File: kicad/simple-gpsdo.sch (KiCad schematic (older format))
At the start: 93 parts, among them J1 PPS_OUT, J2 PWR, J3 ISP, J6 USB_B_Micro, J7 NEO-6M, J8 10MHz_OUT, Q1 PJA3407, SW1 RST, U1 XRP6272ITC5TR-F, U2 ATmega32U4-AU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

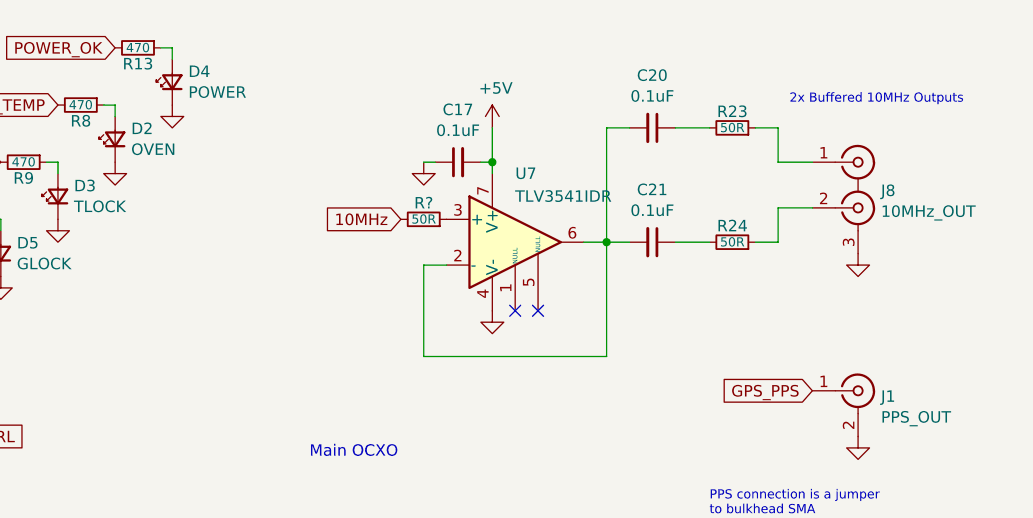
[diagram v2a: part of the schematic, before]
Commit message: final schematic updates for new buffer amplifier
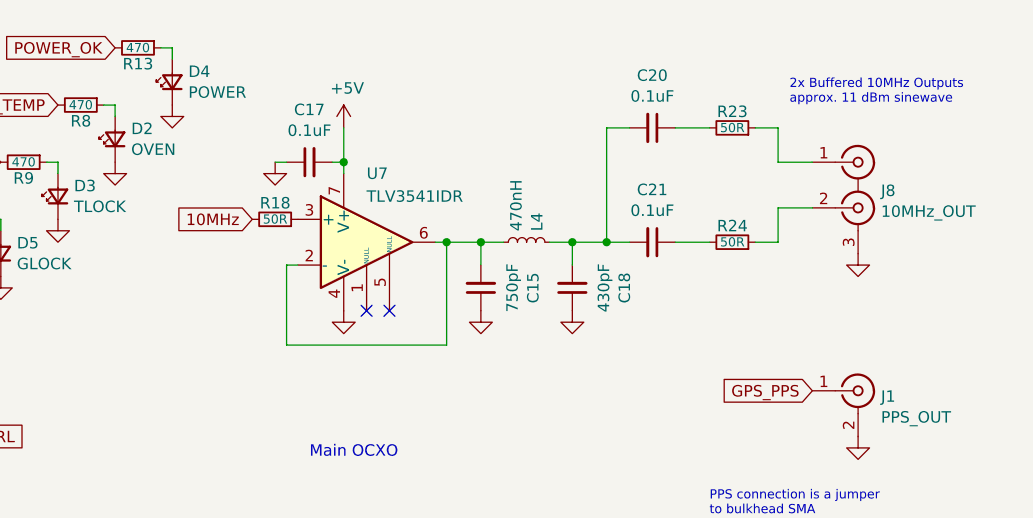
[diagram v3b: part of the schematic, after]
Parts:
- added C15: 750pF, Capacitor_SMD:C_0805_2012Metric_Pad1.15x1.40mm_HandSolder, symbol Device:C_Small
- added C18: 430pF, Capacitor_SMD:C_0805_2012Metric_Pad1.15x1.40mm_HandSolder, symbol Device:C_Small
- added L4: 470nH, Inductor_SMD:L_1206_3216Metric_Pad1.42x1.75mm_HandSolder, symbol Device:L_Small
- gave numbers to parts that had none: 1
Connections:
- net GND: now also C15.1, C18.1
- net at U7.2 (-), U7.6: now also C15.2, L4.2; no longer C20.2, C21.2
- new net: C18.2, C20.2, C21.2, L4.1
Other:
- note added: "2x Buffered 10MHz Outputs\napprox. 11 dBm sinewave"
- note removed: "2x Buffered 10MHz Outputs"
- moved on the sheet: C17, R18, U7
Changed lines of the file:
@@
 L Amplifier_Operational:AD8610 U7
 U 1 1 5F779082
-P 8000 1850
-F 0 "U7" H 8000 2150 50  0000 L CNN
-F 1 "TLV3541IDR" H 8000 2050 50  0000 L CNN
-F 2 "Package_SO:SOIC-8_3.9x4.9mm_P1.27mm" H 8050 1900 50  0001 C CNN
-F 3 "https://www.analog.com/media/en/technical-documentation/data-sheets/AD8610_8620.pdf" H 8150 2000 50  0001 C CNN
-	1    8000 1850
+P 7350 1850
+F 0 "U7" H 7350 2150 50  0000 L CNN
+F 1 "TLV3541IDR" H 7350 2050 50  0000 L CNN
+F 2 "Package_SO:SOIC-8_3.9x4.9mm_P1.27mm" H 7400 1900 50  0001 C CNN
+F 3 "https://www.analog.com/media/en/technical-documentation/data-sheets/AD8610_8620.pdf" H 7500 2000 50  0001 C CNN
+	1    7350 1850
 	1    0    0    -1
 $EndComp
@@
 L power:GND #PWR043
 U 1 1 5F857189
-P 7600 1500
-F 0 "#PWR043" H 7600 1250 50  0001 C CNN
-F 1 "GND" H 7605 1327 50  0001 C CNN
-F 2 "" H 7600 1500 50  0001 C CNN
-F 3 "" H 7600 1500 50  0001 C CNN
-	1    7600 1500
+P 6950 1500
+F 0 "#PWR043" H 6950 1250 50  0001 C CNN
+F 1 "GND" H 6955 1327 50  0001 C CNN
+F 2 "" H 6950 1500 50  0001 C CNN
+F 3 "" H 6950 1500 50  0001 C CNN
+	1    6950 1500
 	1    0    0    -1
 $EndComp
@@
 L Device:C_Small C17
 U 1 1 5F87C209
-P 7750 1500
-F 0 "C17" V 7521 1500 50  0000 C CNN
-F 1 "0.1uF" V 7612 1500 50  0000 C CNN
-F 2 "Capacitor_SMD:C_0805_2012Metric_Pad1.15x1.40mm_HandSolder" H 7750 1500 50  0001 C CNN
-F 3 "~" H 7750 1500 50  0001 C CNN
-	1    7750 1500
+P 7100 1500
+F 0 "C17" V 6871 1500 50  0000 C CNN
+F 1 "0.1uF" V 6962 1500 50  0000 C CNN
+F 2 "Capacitor_SMD:C_0805_2012Metric_Pad1.15x1.40mm_HandSolder" H 7100 1500 50  0001 C CNN
+F 3 "~" H 7100 1500 50  0001 C CNN
+	1    7100 1500
 	0    -1   1    0
 $EndComp
 Wire Wire Line
-	7850 1500 7900 1500
-Connection ~ 7900 1500
-Wire Wire Line
-	7900 1500 7900 1550
-Wire Wire Line
-	7650 1500 7600 1500
-Wire Wire Line
-	7900 1350 7900 1500
-NoConn ~ 8000 2150
-NoConn ~ 8100 2150
+	7200 1500 7250 1500
+Connection ~ 7250 1500
+Wire Wire Line
+	7250 1500 7250 1550
+Wire Wire Line
+	7000 1500 6950 1500
+Wire Wire Line
+	7250 1350 7250 1500
+NoConn ~ 7350 2150
+NoConn ~ 7450 2150
 $Comp
 L power:GND #PWR047
 U 1 1 5F8AD7B0
-P 7900 2150
-F 0 "#PWR047" H 7900 1900 50  0001 C CNN
-F 1 "GND" H 7905 1977 50  0001 C CNN
-F 2 "" H 7900 2150 50  0001 C CNN
-F 3 "" H 7900 2150 50  0001 C CNN
-	1    7900 2150
-	1    0    0    -1
-$EndComp
-Wire Wire Line
-	8400 1850 8300 1850
+P 7250 2150
+F 0 "#PWR047" H 7250 1900 50  0001 C CNN
+F 1 "GND" H 7255 1977 50  0001 C CNN
+F 2 "" H 7250 2150 50  0001 C CNN
+F 3 "" H 7250 2150 50  0001 C CNN
+	1    7250 2150
+	1    0    0    -1
+$EndComp
 $Comp
 L Device:C_Small C21
@@
 	0    1    1    0
 $EndComp
-Connection ~ 8400 1850
 Wire Wire Line
 	8400 1350 8400 1850
@@
 	9150 1850 9050 1850
 Text Notes 9200 1250 0    40   ~ 0
-2x Buffered 10MHz Outputs
+2x Buffered 10MHz Outputs\napprox. 11 dBm sinewave
 Text Notes 6750 4850 0    40   ~ 0
 100Ω resistors on all digital lines\nto keep the noise down
@@
 L power:+5V #PWR021
 U 1 1 619B5C48
-P 7900 1350
-F 0 "#PWR021" H 7900 1200 50  0001 C CNN
-F 1 "+5V" H 7915 1523 50  0000 C CNN
-F 2 "" H 7900 1350 50  0001 C CNN
-F 3 "" H 7900 1350 50  0001 C CNN
-	1    7900 1350
+P 7250 1350
+F 0 "#PWR021" H 7250 1200 50  0001 C CNN
+F 1 "+5V" H 7265 1523 50  0000 C CNN
+F 2 "" H 7250 1350 50  0001 C CNN
+F 3 "" H 7250 1350 50  0001 C CNN
+	1    7250 1350
 	1    0    0    -1
 $EndComp
@@
 Wire Wire Line
 	2500 1950 2500 2100
-Text GLabel 7500 1750 0    50   Input ~ 0
+Text GLabel 6850 1750 0    50   Input ~ 0
 10MHz
-Wire Wire Line
-	7600 1950 7700 1950
-Wire Wire Line
-	7600 1950 7600 2350
-Wire Wire Line
-	7600 2350 8400 2350
-Wire Wire Line
-	8400 2350 8400 1850
-$Comp
-L Device:R_Small R?
+$Comp
+L Device:R_Small R18
 U 1 1 618E603F
-P 7600 1750
-F 0 "R?" V 7700 1750 50  0000 C BNN
-F 1 "50R" V 7600 1750 40  0000 C CNN
-F 2 "Resistor_SMD:R_0805_2012Metric_Pad1.15x1.40mm_HandSolder" H 7600 1750 50  0001 C CNN
-F 3 "~" H 7600 1750 50  0001 C CNN
-	1    7600 1750
+P 6950 1750
+F 0 "R18" V 7050 1750 50  0000 C BNN
+F 1 "50R" V 6950 1750 40  0000 C CNN
+F 2 "Resistor_SMD:R_0805_2012Metric_Pad1.15x1.40mm_HandSolder" H 6950 1750 50  0001 C CNN
+F 3 "~" H 6950 1750 50  0001 C CNN
+	1    6950 1750
 	0    1    -1   0
 $EndComp
+Wire Wire Line
+	7650 1850 7700 1850
+Wire Wire Line
+	7700 1850 7700 2300
+Wire Wire Line
+	7700 2300 7000 2300
+Wire Wire Line
+	7000 2300 7000 1950
+Wire Wire Line
+	7000 1950 7050 1950
+$Comp
+L Device:C_Small C15
+U 1 1 618C0510
+P 7850 2050
+F 0 "C15" V 7621 2050 50  0000 C CNN
+F 1 "750pF" V 7712 2050 50  0000 C CNN
+F 2 "Capacitor_SMD:C_0805_2012Metric_Pad1.15x1.40mm_HandSolder" H 7850 2050 50  0001 C CNN
+F 3 "~" H 7850 2050 50  0001 C CNN
+	1    7850 2050
+	-1   0    0    1
+$EndComp
+$Comp
+L Device:C_Small C18
+U 1 1 618C1226
+P 8250 2050
+F 0 "C18" V 8021 2050 50  0000 C CNN
+F 1 "430pF" V 8112 2050 50  0000 C CNN
+F 2 "Capacitor_SMD:C_0805_2012Metric_Pad1.15x1.40mm_HandSolder" H 8250 2050 50  0001 C CNN
+F 3 "~" H 8250 2050 50  0001 C CNN
+	1    8250 2050
+	-1   0    0    1
+$EndComp
+$Comp
+L power:GND #PWR042
+U 1 1 618C1B7E
+P 8250 2150
+F 0 "#PWR042" H 8250 1900 50  0001 C CNN
+F 1 "GND" H 8255 1977 50  0001 C CNN
+F 2 "" H 8250 2150 50  0001 C CNN
+F 3 "" H 8250 2150 50  0001 C CNN
+	1    8250 2150
+	1    0    0    -1
+$EndComp
+$Comp
+L power:GND #PWR040
+U 1 1 618C21E8
+P 7850 2150
+F 0 "#PWR040" H 7850 1900 50  0001 C CNN
+F 1 "GND" H 7855 1977 50  0001 C CNN
+F 2 "" H 7850 2150 50  0001 C CNN
+F 3 "" H 7850 2150 50  0001 C CNN
+	1    7850 2150
+	1    0    0    -1
+$EndComp
+$Comp
+L Device:L_Small L4
+U 1 1 618C4152
+P 8050 1850
+F 0 "L4" H 8098 1896 50  0000 L CNN
+F 1 "470nH" H 8098 1805 50  0000 L CNN
+F 2 "Inductor_SMD:L_1206_3216Metric_Pad1.42x1.75mm_HandSolder" H 8050 1850 50  0001 C CNN
+F 3 "~" H 8050 1850 50  0001 C CNN
+	1    8050 1850
+	0    1    -1   0
+$EndComp
+Wire Wire Line
+	8150 1850 8250 1850
+Connection ~ 8400 1850
+Wire Wire Line
+	8250 1950 8250 1850
+Connection ~ 8250 1850
+Wire Wire Line
+	8250 1850 8400 1850
+Wire Wire Line
+	7850 1950 7850 1850
+Wire Wire Line
+	7850 1850 7700 1850
+Connection ~ 7700 1850
+Wire Wire Line
+	7850 1850 7950 1850
+Connection ~ 7850 1850
 $EndSCHEMATC

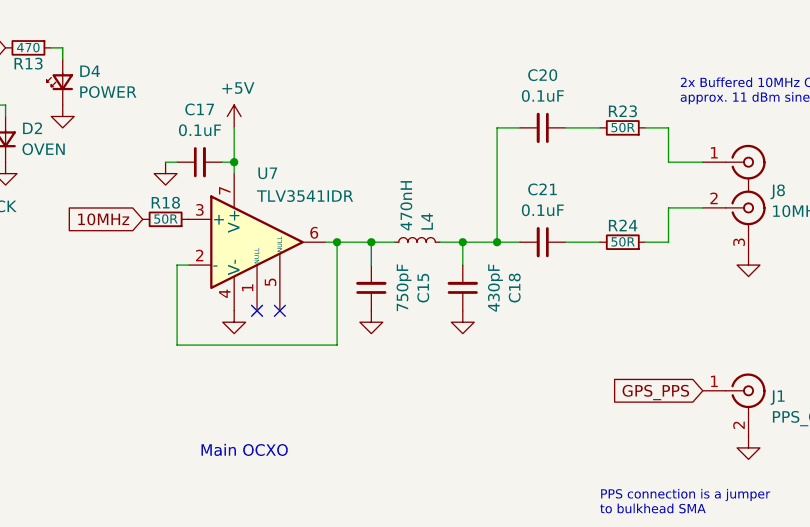
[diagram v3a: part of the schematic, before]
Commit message: more simulation stuff, changed output filter
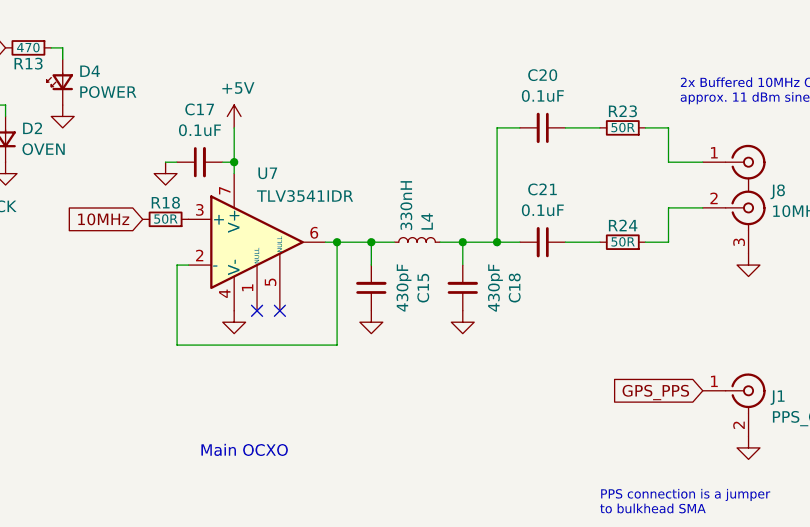
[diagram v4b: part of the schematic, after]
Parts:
- C15: value 750pF -> 430pF
- L4: value 470nH -> 330nH
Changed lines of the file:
@@
 P 7850 2050
 F 0 "C15" V 7621 2050 50  0000 C CNN
-F 1 "750pF" V 7712 2050 50  0000 C CNN
+F 1 "430pF" V 7712 2050 50  0000 C CNN
 F 2 "Capacitor_SMD:C_0805_2012Metric_Pad1.15x1.40mm_HandSolder" H 7850 2050 50  0001 C CNN
 F 3 "~" H 7850 2050 50  0001 C CNN
@@
 P 8050 1850
 F 0 "L4" H 8098 1896 50  0000 L CNN
-F 1 "470nH" H 8098 1805 50  0000 L CNN
+F 1 "330nH" H 8098 1805 50  0000 L CNN
 F 2 "Inductor_SMD:L_1206_3216Metric_Pad1.42x1.75mm_HandSolder" H 8050 1850 50  0001 C CNN
 F 3 "~" H 8050 1850 50  0001 C CNN

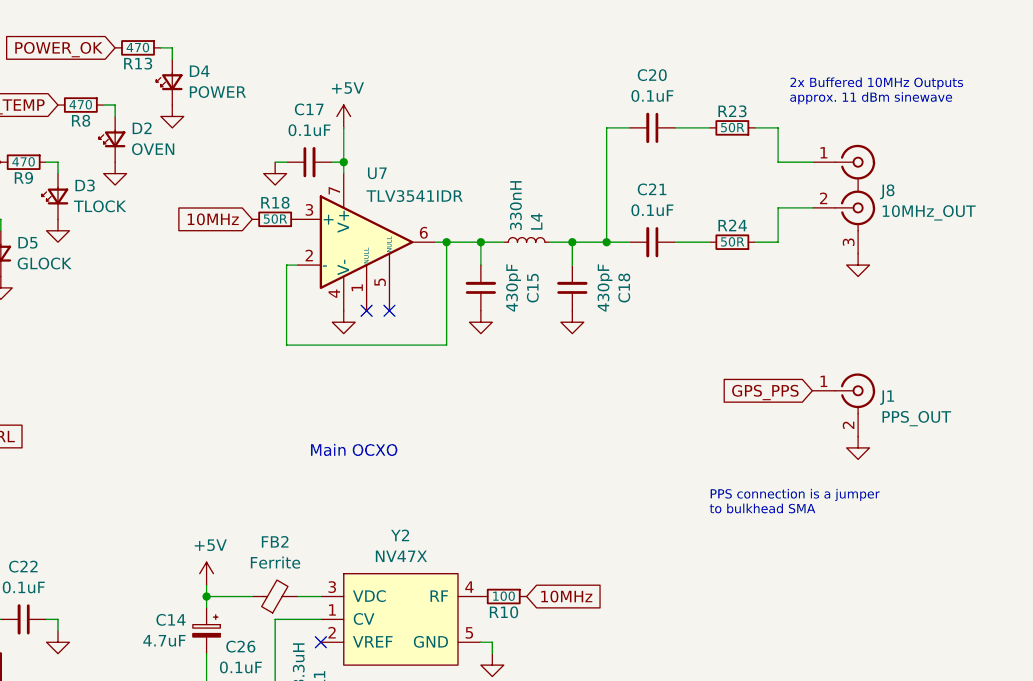
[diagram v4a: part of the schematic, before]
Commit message: finalized output amplifier design
added wilkinson divider for dual outputs to improve isolation and amplitude
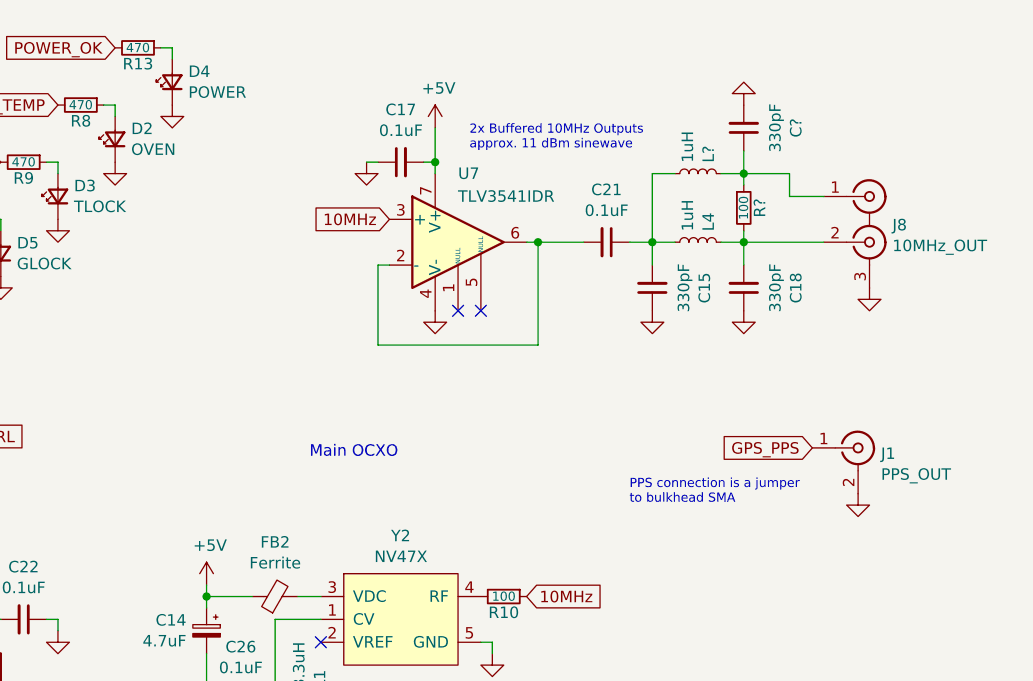
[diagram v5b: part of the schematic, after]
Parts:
- removed C20: 0.1uF, Capacitor_SMD:C_0805_2012Metric_Pad1.15x1.40mm_HandSolder, symbol Device:C_Small
- removed R18, R23, R24: 50R, Resistor_SMD:R_0805_2012Metric_Pad1.15x1.40mm_HandSolder, symbol Device:R_Small
- added C?: 330pF, Capacitor_SMD:C_0805_2012Metric_Pad1.15x1.40mm_HandSolder, symbol Device:C_Small
- added L?: 1uH, Inductor_SMD:L_1206_3216Metric_Pad1.42x1.75mm_HandSolder, symbol Device:L_Small
- added R?: 100, Resistor_SMD:R_0805_2012Metric_Pad1.15x1.40mm_HandSolder, symbol Device:R_Small
- C15, C18: value 430pF -> 330pF
- L4: value 330nH -> 1uH
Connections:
- net 10MHz: now also U7.3 (+)
- net GND: now also C?.2
- net at U7.2 (-), U7.6: now also C21.2; no longer C15.2, L4.2
- net at C21.1: now also C15.2, L4.2, L?.2
- net at C18.2, L4.1: now also J8.2 (IN2), R?.2; no longer C21.2
- net at J8.1 (IN1): now also C?.1, L?.1, R?.1
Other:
- moved on the sheet: C15, C17, C18, C21, J1, J8, L4, U7

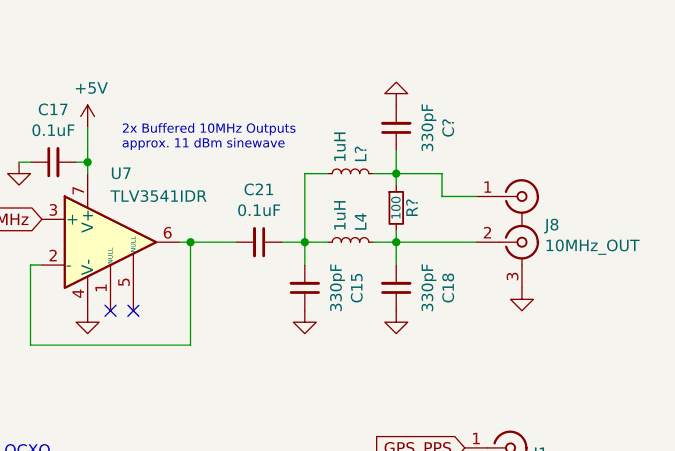
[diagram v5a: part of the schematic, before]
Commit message: more schematic and pcb updates
finished 10MHz output and fixed LED orientation
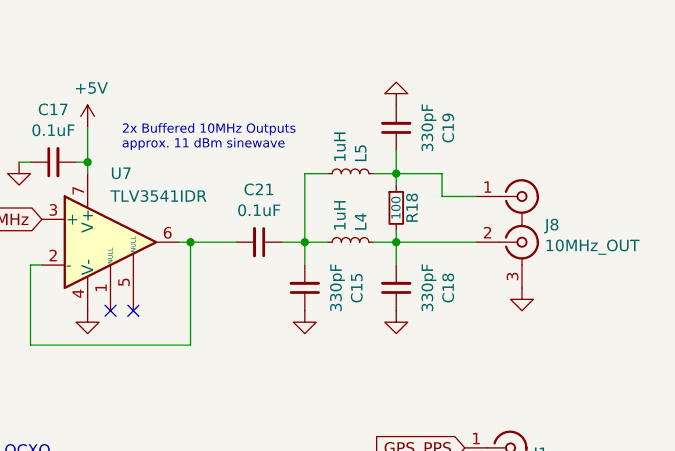
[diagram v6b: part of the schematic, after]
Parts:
- D2, D3, D4, D5, D6: footprint LED_THT:LED_D3.0mm_Horizontal_O1.27mm_Z2.0mm_Clear -> LED_THT_CUSTOM:LED_D3.0mm_Horizontal_O1.27mm_Z2.0mm
- U5: footprint Package_TO_SOT_SMD:SOT-23 -> Package_TO_SOT_SMD:SOT-23_Handsoldering
- gave numbers to parts that had none: 3
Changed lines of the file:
@@
 Sheet 1 1
 Title "Simple GPSDO"
-Date "2021-11-04"
+Date "2021-11-06"
 Rev "E"
 Comp "W3AXL"
@@
 F 0 "D5" V 5796 1830 50  0000 R CNN
 F 1 "GLOCK" V 5705 1830 50  0000 R CNN
-F 2 "LED_THT:LED_D3.0mm_Horizontal_O1.27mm_Z2.0mm_Clear" V 5750 1900 50  0001 C CNN
+F 2 "LED_THT_CUSTOM:LED_D3.0mm_Horizontal_O1.27mm_Z2.0mm" V 5750 1900 50  0001 C CNN
 F 3 "~" V 5750 1900 50  0001 C CNN
 	1    5750 1900
@@
 F 0 "D3" V 6046 1580 50  0000 R CNN
 F 1 "TLOCK" V 5955 1580 50  0000 R CNN
-F 2 "LED_THT:LED_D3.0mm_Horizontal_O1.27mm_Z2.0mm_Clear" V 6000 1650 50  0001 C CNN
+F 2 "LED_THT_CUSTOM:LED_D3.0mm_Horizontal_O1.27mm_Z2.0mm" V 6000 1650 50  0001 C CNN
 F 3 "~" V 6000 1650 50  0001 C CNN
 	1    6000 1650
@@
 F 0 "D2" V 6296 1330 50  0000 R CNN
 F 1 "OVEN" V 6205 1330 50  0000 R CNN
-F 2 "LED_THT:LED_D3.0mm_Horizontal_O1.27mm_Z2.0mm_Clear" V 6250 1400 50  0001 C CNN
+F 2 "LED_THT_CUSTOM:LED_D3.0mm_Horizontal_O1.27mm_Z2.0mm" V 6250 1400 50  0001 C CNN
 F 3 "~" V 6250 1400 50  0001 C CNN
 	1    6250 1400
@@
 F 0 "D4" V 6546 1080 50  0000 R CNN
 F 1 "POWER" V 6455 1080 50  0000 R CNN
-F 2 "LED_THT:LED_D3.0mm_Horizontal_O1.27mm_Z2.0mm_Clear" V 6500 1150 50  0001 C CNN
+F 2 "LED_THT_CUSTOM:LED_D3.0mm_Horizontal_O1.27mm_Z2.0mm" V 6500 1150 50  0001 C CNN
 F 3 "~" V 6500 1150 50  0001 C CNN
 	1    6500 1150
@@
 F 0 "D6" V 5546 2080 50  0000 R CNN
 F 1 "PPS" V 5455 2080 50  0000 R CNN
-F 2 "LED_THT:LED_D3.0mm_Horizontal_O1.27mm_Z2.0mm_Clear" V 5500 2150 50  0001 C CNN
+F 2 "LED_THT_CUSTOM:LED_D3.0mm_Horizontal_O1.27mm_Z2.0mm" V 5500 2150 50  0001 C CNN
 F 3 "~" V 5500 2150 50  0001 C CNN
 	1    5500 2150
@@
 F 0 "U5" H 2050 2066 50  0000 C CNN
 F 1 "LM4041QDIM3-1.2" H 2050 1975 50  0000 C CNN
-F 2 "Package_TO_SOT_SMD:SOT-23" H 2050 1650 50  0001 C CIN
+F 2 "Package_TO_SOT_SMD:SOT-23_Handsoldering" H 2050 1650 50  0001 C CIN
 F 3 "http://www.ti.com/lit/ds/symlink/lm4040-n.pdf" H 2050 1850 50  0001 C CIN
 	1    2050 1850
@@
 	8900 1850 9000 1850
 $Comp
-L Device:L_Small L?
+L Device:L_Small L5
 U 1 1 6198FDFF
 P 8800 1550
-F 0 "L?" H 8848 1596 50  0000 L CNN
+F 0 "L5" H 8848 1596 50  0000 L CNN
 F 1 "1uH" H 8848 1505 50  0000 L CNN
 F 2 "Inductor_SMD:L_1206_3216Metric_Pad1.42x1.75mm_HandSolder" H 8800 1550 50  0001 C CNN
@@
 $EndComp
 $Comp
-L Device:C_Small C?
+L Device:C_Small C19
 U 1 1 619905C0
 P 9000 1350
-F 0 "C?" V 8771 1350 50  0000 C CNN
+F 0 "C19" V 8771 1350 50  0000 C CNN
 F 1 "330pF" V 8862 1350 50  0000 C CNN
 F 2 "Capacitor_SMD:C_0805_2012Metric_Pad1.15x1.40mm_HandSolder" H 9000 1350 50  0001 C CNN
@@
 	9000 1550 8900 1550
 $Comp
-L power:GND #PWR?
+L power:GND #PWR045
 U 1 1 619EC479
 P 9000 1250
-F 0 "#PWR?" H 9000 1000 50  0001 C CNN
+F 0 "#PWR045" H 9000 1000 50  0001 C CNN
 F 1 "GND" H 9005 1077 50  0001 C CNN
 F 2 "" H 9000 1250 50  0001 C CNN
@@
 $EndComp
 $Comp
-L Device:R_Small R?
+L Device:R_Small R18
 U 1 1 619EED4F
 P 9000 1700
-F 0 "R?" V 9100 1700 50  0000 C BNN
+F 0 "R18" V 9100 1700 50  0000 C BNN
 F 1 "100" V 9000 1700 40  0000 C CNN
 F 2 "Resistor_SMD:R_0805_2012Metric_Pad1.15x1.40mm_HandSolder" H 9000 1700 50  0001 C CNN

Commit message: schematic for rev E finalized
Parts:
- R30: value 10k -> 3k9
- U5: value LM4041QDIM3-1.2 -> LM4041DFTA
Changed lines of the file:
@@
 P 2050 1850
 F 0 "U5" H 2050 2066 50  0000 C CNN
-F 1 "LM4041QDIM3-1.2" H 2050 1975 50  0000 C CNN
+F 1 "LM4041DFTA" H 2050 1975 50  0000 C CNN
 F 2 "Package_TO_SOT_SMD:SOT-23_Handsoldering" H 2050 1650 50  0001 C CIN
 F 3 "http://www.ti.com/lit/ds/symlink/lm4040-n.pdf" H 2050 1850 50  0001 C CIN
@@
 P 2500 1700
 F 0 "R30" V 2600 1700 50  0000 C BNN
-F 1 "10k" V 2500 1700 40  0000 C CNN
+F 1 "3k9" V 2500 1700 40  0000 C CNN
 F 2 "Resistor_SMD:R_0805_2012Metric_Pad1.15x1.40mm_HandSolder" H 2500 1700 50  0001 C CNN
 F 3 "~" H 2500 1700 50  0001 C CNN
